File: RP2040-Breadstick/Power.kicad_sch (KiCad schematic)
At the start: 5 parts

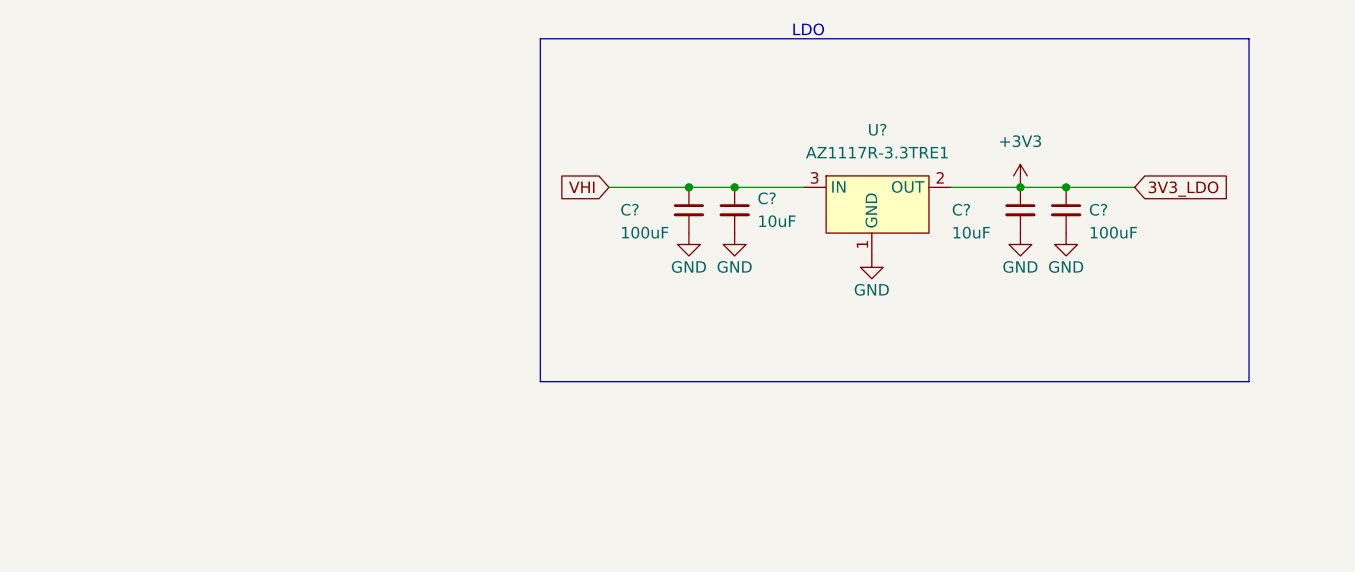
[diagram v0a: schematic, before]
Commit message: IMU Pins and Power Supply updated
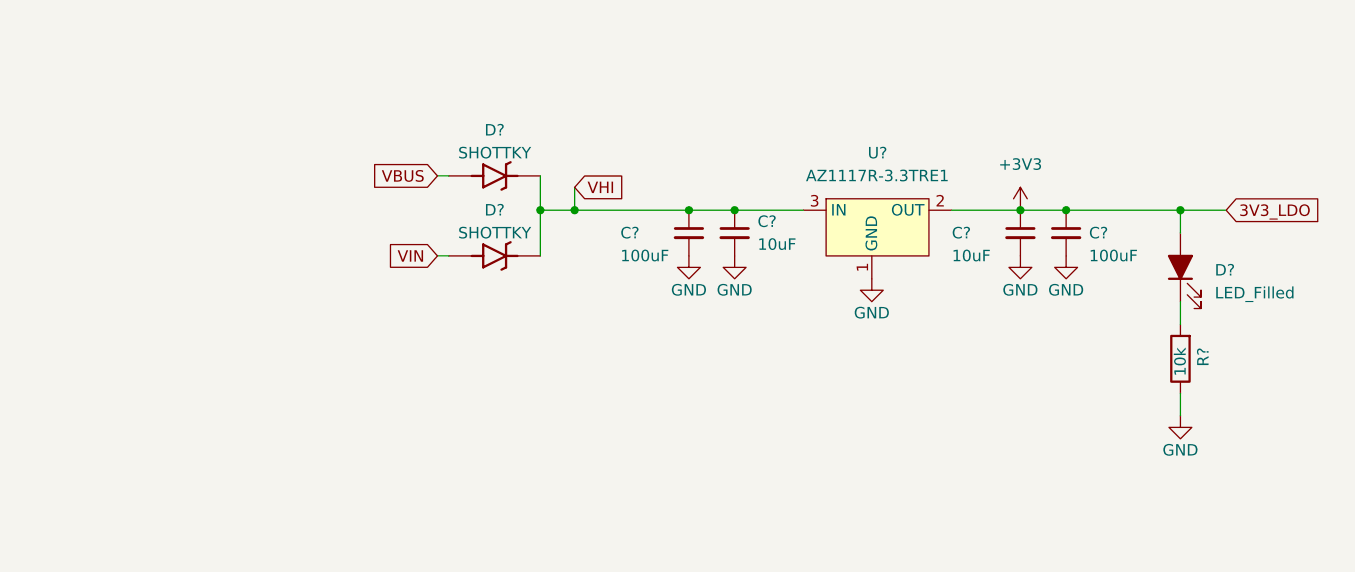
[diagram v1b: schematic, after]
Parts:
- added D? (x2): SHOTTKY, Diode_SMD:D_SOD-123, symbol SparkFun-DiscreteSemi:DIODE-SHOTTKY_MBRA140
- added D?: LED_Filled, LED_SMD:LED_0805_2012Metric, symbol Device:LED_Filled
- added R?: 10k, Breadstick Footprints:Perfect_0402_Resistor, symbol Device:R
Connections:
- net +3V3: now also D?.2 (A)
- net GND: now also R?.1
- net VHI: now also D?.1 (C), D?.1 (C)
- new net: D?.1 (K), R?.2
- new net VBUS: D?.2 (A)
- new net VIN: D?.2 (A)
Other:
- note removed: "LDO"
- moved on the sheet: C?, U?

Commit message: Schematic Rough Draft Complete
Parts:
- gave numbers to parts that had none: 9
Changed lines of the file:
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@@
   (symbol (lib_id "Device:C_Small") (at 137.16 97.79 0) (unit 1)
     (in_bom yes) (on_board yes)
-    (property "Reference" "C?" (id 0) (at 139.7 96.52 0)
+    (property "Reference" "C502" (id 0) (at 139.7 96.52 0)
       (effects (font (size 1.27 1.27)) (justify left))
     )
@@
   (symbol (lib_id "Device:C_Small") (at 168.91 97.79 0) (unit 1)
     (in_bom yes) (on_board yes)
-    (property "Reference" "C?" (id 0) (at 161.29 97.79 0)
+    (property "Reference" "C503" (id 0) (at 161.29 97.79 0)
       (effects (font (size 1.27 1.27)) (justify left))
     )
@@
   (symbol (lib_id "Device:R") (at 186.69 111.76 180) (unit 1)
     (in_bom yes) (on_board yes)
-    (property "Reference" "R?" (id 0) (at 189.23 110.49 90)
+    (property "Reference" "R501" (id 0) (at 189.23 110.49 90)
       (effects (font (size 1.27 1.27)) (justify left))
     )
@@
   (symbol (lib_id "power:GND") (at 132.08 100.33 0) (unit 1)
     (in_bom yes) (on_board yes)
-    (property "Reference" "#PWR?" (id 0) (at 132.08 106.68 0)
+    (property "Reference" "#PWR0502" (id 0) (at 132.08 106.68 0)
       (effects (font (size 1.27 1.27)) hide)
     )
@@
   (symbol (lib_id "power:GND") (at 173.99 100.33 0) (unit 1)
     (in_bom yes) (on_board yes)
-    (property "Reference" "#PWR?" (id 0) (at 173.99 106.68 0)
+    (property "Reference" "#PWR0505" (id 0) (at 173.99 106.68 0)
       (effects (font (size 1.27 1.27)) hide)
     )
@@
   (symbol (lib_name "DIODE-SHOTTKY_MBRA140_1") (lib_id "SparkFun-DiscreteSemi:DIODE-SHOTTKY_MBRA140") (at 110.49 91.44 0) (unit 1)
     (in_bom yes) (on_board yes)
-    (property "Reference" "D?" (id 0) (at 110.49 86.36 0))
+    (property "Reference" "D501" (id 0) (at 110.49 86.36 0))
     (property "Value" "SHOTTKY" (id 1) (at 110.49 88.9 0))
     (property "Footprint" "Diode_SMD:D_SOD-123" (id 2) (at 127 95.25 0)
@@
   (symbol (lib_id "Device:C_Small") (at 173.99 97.79 0) (unit 1)
     (in_bom yes) (on_board yes)
-    (property "Reference" "C?" (id 0) (at 176.53 97.79 0)
+    (property "Reference" "C504" (id 0) (at 176.53 97.79 0)
       (effects (font (size 1.27 1.27)) (justify left))
     )
@@
   (symbol (lib_name "DIODE-SHOTTKY_MBRA140_1") (lib_id "SparkFun-DiscreteSemi:DIODE-SHOTTKY_MBRA140") (at 110.49 100.33 0) (unit 1)
     (in_bom yes) (on_board yes)
-    (property "Reference" "D?" (id 0) (at 110.49 95.25 0))
+    (property "Reference" "D502" (id 0) (at 110.49 95.25 0))
     (property "Value" "SHOTTKY" (id 1) (at 110.49 97.79 0))
     (property "Footprint" "Diode_SMD:D_SOD-123" (id 2) (at 127 104.14 0)
@@
   (symbol (lib_id "power:GND") (at 152.4 102.87 0) (unit 1)
     (in_bom yes) (on_board yes)
-    (property "Reference" "#PWR?" (id 0) (at 152.4 109.22 0)
+    (property "Reference" "#PWR0506" (id 0) (at 152.4 109.22 0)
       (effects (font (size 1.27 1.27)) hide)
     )
@@
   (symbol (lib_id "power:GND") (at 168.91 100.33 0) (unit 1)
     (in_bom yes) (on_board yes)
-    (property "Reference" "#PWR?" (id 0) (at 168.91 106.68 0)
+    (property "Reference" "#PWR0504" (id 0) (at 168.91 106.68 0)
       (effects (font (size 1.27 1.27)) hide)
     )
@@
   (symbol (lib_id "power:GND") (at 137.16 100.33 0) (unit 1)
     (in_bom yes) (on_board yes)
-    (property "Reference" "#PWR?" (id 0) (at 137.16 106.68 0)
+    (property "Reference" "#PWR0503" (id 0) (at 137.16 106.68 0)
       (effects (font (size 1.27 1.27)) hide)
     )
@@
   (symbol (lib_id "power:+3V3") (at 168.91 95.25 0) (unit 1)
     (in_bom yes) (on_board yes) (fields_autoplaced)
-    (property "Reference" "#PWR?" (id 0) (at 168.91 99.06 0)
+    (property "Reference" "#PWR0501" (id 0) (at 168.91 99.06 0)
       (effects (font (size 1.27 1.27)) hide)
     )
@@
   (symbol (lib_id "BreadstickLibrary:AZ1117R-3.3TRE1") (at 152.4 96.52 0) (unit 1)
     (in_bom yes) (on_board yes) (fields_autoplaced)
-    (property "Reference" "U?" (id 0) (at 153.035 88.9 0))
+    (property "Reference" "U501" (id 0) (at 153.035 88.9 0))
     (property "Value" "AZ1117R-3.3TRE1" (id 1) (at 153.035 91.44 0))
     (property "Footprint" "Package_TO_SOT_SMD:SOT-89-3" (id 2) (at 152.4 96.52 0)
@@
   (symbol (lib_id "power:GND") (at 186.69 118.11 0) (unit 1)
     (in_bom yes) (on_board yes)
-    (property "Reference" "#PWR?" (id 0) (at 186.69 124.46 0)
+    (property "Reference" "#PWR0507" (id 0) (at 186.69 124.46 0)
       (effects (font (size 1.27 1.27)) hide)
     )
@@
   (symbol (lib_id "Device:C_Small") (at 132.08 97.79 0) (unit 1)
     (in_bom yes) (on_board yes)
-    (property "Reference" "C?" (id 0) (at 124.46 97.79 0)
+    (property "Reference" "C501" (id 0) (at 124.46 97.79 0)
       (effects (font (size 1.27 1.27)) (justify left))
     )
@@
   (symbol (lib_id "Device:LED_Filled") (at 186.69 101.6 90) (unit 1)
     (in_bom yes) (on_board yes) (fields_autoplaced)
-    (property "Reference" "D?" (id 0) (at 190.5 101.9174 90)
+    (property "Reference" "D503" (id 0) (at 190.5 101.9174 90)
       (effects (font (size 1.27 1.27)) (justify right))
     )

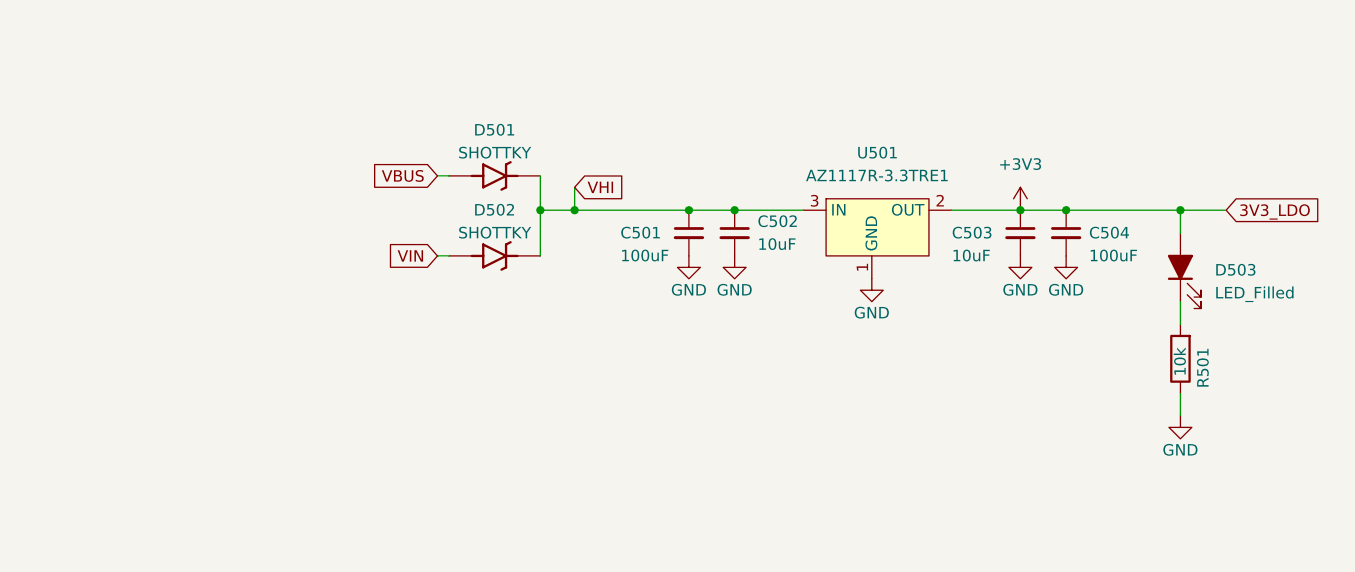
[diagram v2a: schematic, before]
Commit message: Initial PCB organization complete.
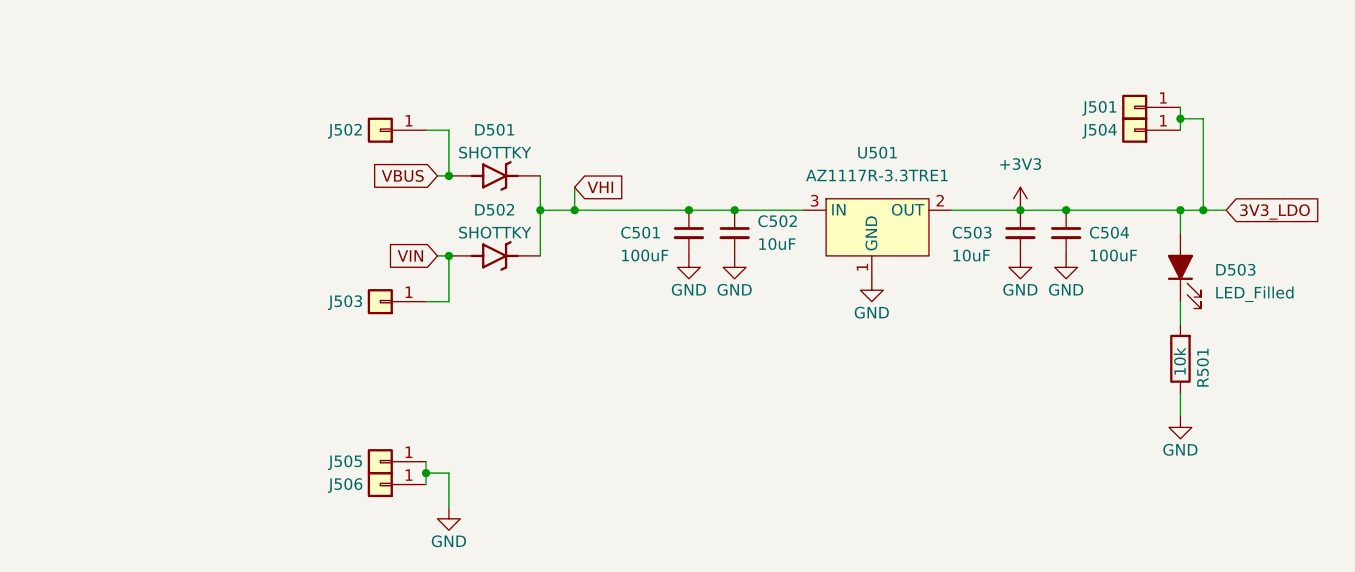
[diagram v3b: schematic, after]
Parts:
- added J501, J502, J503, J504, J505, J506: Conn_01x01, Connector_PinHeader_2.54mm:PinHeader_1x01_P2.54mm_Vertical, symbol Connector_Generic:Conn_01x01
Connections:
- net +3V3: now also J501.1 (Pin_1), J504.1 (Pin_1)
- net GND: now also J505.1 (Pin_1), J506.1 (Pin_1)
- net VBUS: now also J502.1 (Pin_1)
- net VIN: now also J503.1 (Pin_1)
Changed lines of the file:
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@@
   (junction (at 186.69 95.25) (diameter 0) (color 0 0 0 0)
   )
+  (junction (at 186.69 85.09) (diameter 0) (color 0 0 0 0)
+  )
   (junction (at 168.91 95.25) (diameter 0) (color 0 0 0 0)
   )
   (junction (at 137.16 95.25) (diameter 0) (color 0 0 0 0)
   )
+  (junction (at 105.41 91.44) (diameter 0) (color 0 0 0 0)
+  )
+  (junction (at 189.23 95.25) (diameter 0) (color 0 0 0 0)
+  )
+  (junction (at 105.41 100.33) (diameter 0) (color 0 0 0 0)
+  )
+  (junction (at 102.87 124.46) (diameter 0) (color 0 0 0 0)
+  )
   (junction (at 115.57 95.25) (diameter 0) (color 0 0 0 0)
   )
   (junction (at 132.08 95.25) (diameter 0) (color 0 0 0 0)
   )
-  (wire (pts (xy 186.69 95.25) (xy 191.77 95.25))
+  (wire (pts (xy 186.69 85.09) (xy 186.69 86.36))
+    (stroke (width 0) (type default) (color 0 0 0 0))
+  )
+  (wire (pts (xy 102.87 124.46) (xy 102.87 125.73))
+    (stroke (width 0) (type default) (color 0 0 0 0))
+  )
+  (wire (pts (xy 186.69 95.25) (xy 189.23 95.25))
     (stroke (width 0) (type default) (color 0 0 0 0))
   )
@@
     (stroke (width 0) (type default) (color 0 0 0 0))
   )
+  (wire (pts (xy 186.69 83.82) (xy 186.69 85.09))
+    (stroke (width 0) (type default) (color 0 0 0 0))
+  )
+  (wire (pts (xy 105.41 100.33) (xy 105.41 105.41))
+    (stroke (width 0) (type default) (color 0 0 0 0))
+  )
+  (wire (pts (xy 105.41 124.46) (xy 102.87 124.46))
+    (stroke (width 0) (type default) (color 0 0 0 0))
+  )
+  (wire (pts (xy 186.69 85.09) (xy 189.23 85.09))
+    (stroke (width 0) (type default) (color 0 0 0 0))
+  )
   (wire (pts (xy 115.57 95.25) (xy 115.57 100.33))
     (stroke (width 0) (type default) (color 0 0 0 0))
   )
+  (wire (pts (xy 102.87 105.41) (xy 105.41 105.41))
+    (stroke (width 0) (type default) (color 0 0 0 0))
+  )
+  (wire (pts (xy 189.23 85.09) (xy 189.23 95.25))
+    (stroke (width 0) (type default) (color 0 0 0 0))
+  )
   (wire (pts (xy 119.38 95.25) (xy 132.08 95.25))
     (stroke (width 0) (type default) (color 0 0 0 0))
   )
+  (wire (pts (xy 102.87 86.36) (xy 105.41 86.36))
+    (stroke (width 0) (type default) (color 0 0 0 0))
+  )
+  (wire (pts (xy 189.23 95.25) (xy 191.77 95.25))
+    (stroke (width 0) (type default) (color 0 0 0 0))
+  )
   (wire (pts (xy 186.69 95.25) (xy 186.69 97.79))
     (stroke (width 0) (type default) (color 0 0 0 0))
@@
     (stroke (width 0) (type default) (color 0 0 0 0))
   )
+  (wire (pts (xy 102.87 123.19) (xy 102.87 124.46))
+    (stroke (width 0) (type default) (color 0 0 0 0))
+  )
   (wire (pts (xy 104.14 91.44) (xy 105.41 91.44))
     (stroke (width 0) (type default) (color 0 0 0 0))
@@
   )
   (wire (pts (xy 137.16 95.25) (xy 144.78 95.25))
+    (stroke (width 0) (type default) (color 0 0 0 0))
+  )
+  (wire (pts (xy 105.41 86.36) (xy 105.41 91.44))
+    (stroke (width 0) (type default) (color 0 0 0 0))
+  )
+  (wire (pts (xy 105.41 128.27) (xy 105.41 124.46))
     (stroke (width 0) (type default) (color 0 0 0 0))
   )
@@
     (pin "2")
   )
+  (symbol (lib_id "Connector_Generic:Conn_01x01") (at 97.79 123.19 180) (unit 1)
+    (in_bom yes) (on_board yes)
+    (property "Reference" "J505" (id 0) (at 93.98 123.19 0))
+    (property "Value" "Conn_01x01" (id 1) (at 87.63 123.19 0)
+      (effects (font (size 1.27 1.27)) hide)
+    )
+    (property "Footprint" "Connector_PinHeader_2.54mm:PinHeader_1x01_P2.54mm_Vertical" (id 2) (at 97.79 123.19 0)
+      (effects (font (size 1.27 1.27)) hide)
+    )
+    (property "Datasheet" "~" (id 3) (at 97.79 123.19 0)
+      (effects (font (size 1.27 1.27)) hide)
+    )
+    (property "JLCPCB P/N" "C492400" (id 4) (at 97.79 123.19 0)
+      (effects (font (size 1.27 1.27)) hide)
+    )
+    (pin "1")
+  )
   (symbol (lib_id "Device:C_Small") (at 168.91 97.79 0) (unit 1)
     (in_bom yes) (on_board yes)
@@
     (pin "1")
     (pin "2")
+  )
+  (symbol (lib_id "Connector_Generic:Conn_01x01") (at 97.79 105.41 180) (unit 1)
+    (in_bom yes) (on_board yes)
+    (property "Reference" "J503" (id 0) (at 93.98 105.41 0))
+    (property "Value" "Conn_01x01" (id 1) (at 87.63 105.41 0)
+      (effects (font (size 1.27 1.27)) hide)
+    )
+    (property "Footprint" "Connector_PinHeader_2.54mm:PinHeader_1x01_P2.54mm_Vertical" (id 2) (at 97.79 105.41 0)
+      (effects (font (size 1.27 1.27)) hide)
+    )
+    (property "Datasheet" "~" (id 3) (at 97.79 105.41 0)
+      (effects (font (size 1.27 1.27)) hide)
+    )
+    (property "JLCPCB P/N" "C492400" (id 4) (at 97.79 105.41 0)
+      (effects (font (size 1.27 1.27)) hide)
+    )
+    (pin "1")
+  )
+  (symbol (lib_id "Connector_Generic:Conn_01x01") (at 181.61 83.82 180) (unit 1)
+    (in_bom yes) (on_board yes)
+    (property "Reference" "J501" (id 0) (at 177.8 83.82 0))
+    (property "Value" "Conn_01x01" (id 1) (at 171.45 83.82 0)
+      (effects (font (size 1.27 1.27)) hide)
+    )
+    (property "Footprint" "Connector_PinHeader_2.54mm:PinHeader_1x01_P2.54mm_Vertical" (id 2) (at 181.61 83.82 0)
+      (effects (font (size 1.27 1.27)) hide)
+    )
+    (property "Datasheet" "~" (id 3) (at 181.61 83.82 0)
+      (effects (font (size 1.27 1.27)) hide)
+    )
+    (property "JLCPCB P/N" "C492400" (id 4) (at 181.61 83.82 0)
+      (effects (font (size 1.27 1.27)) hide)
+    )
+    (pin "1")
+  )
+  (symbol (lib_id "Connector_Generic:Conn_01x01") (at 97.79 125.73 180) (unit 1)
+    (in_bom yes) (on_board yes)
+    (property "Reference" "J506" (id 0) (at 93.98 125.73 0))
+    (property "Value" "Conn_01x01" (id 1) (at 87.63 125.73 0)
+      (effects (font (size 1.27 1.27)) hide)
+    )
+    (property "Footprint" "Connector_PinHeader_2.54mm:PinHeader_1x01_P2.54mm_Vertical" (id 2) (at 97.79 125.73 0)
+      (effects (font (size 1.27 1.27)) hide)
+    )
+    (property "Datasheet" "~" (id 3) (at 97.79 125.73 0)
+      (effects (font (size 1.27 1.27)) hide)
+    )
+    (property "JLCPCB P/N" "C492400" (id 4) (at 97.79 125.73 0)
+      (effects (font (size 1.27 1.27)) hide)
+    )
+    (pin "1")
+  )
+  (symbol (lib_id "Connector_Generic:Conn_01x01") (at 181.61 86.36 180) (unit 1)
+    (in_bom yes) (on_board yes)
+    (property "Reference" "J504" (id 0) (at 177.8 86.36 0))
+    (property "Value" "Conn_01x01" (id 1) (at 171.45 86.36 0)
+      (effects (font (size 1.27 1.27)) hide)
+    )
+    (property "Footprint" "Connector_PinHeader_2.54mm:PinHeader_1x01_P2.54mm_Vertical" (id 2) (at 181.61 86.36 0)
+      (effects (font (size 1.27 1.27)) hide)
+    )
+    (property "Datasheet" "~" (id 3) (at 181.61 86.36 0)
+      (effects (font (size 1.27 1.27)) hide)
+    )
+    (property "JLCPCB P/N" "C492400" (id 4) (at 181.61 86.36 0)
+      (effects (font (size 1.27 1.27)) hide)
+    )
+    (pin "1")
   )
   (symbol (lib_id "power:GND") (at 132.08 100.33 0) (unit 1)
@@
     )
     (property "Datasheet" "" (id 3) (at 152.4 102.87 0)
+      (effects (font (size 1.27 1.27)) hide)
+    )
+    (pin "1")
+  )
+  (symbol (lib_id "Connector_Generic:Conn_01x01") (at 97.79 86.36 180) (unit 1)
+    (in_bom yes) (on_board yes)
+    (property "Reference" "J502" (id 0) (at 93.98 86.36 0))
+    (property "Value" "Conn_01x01" (id 1) (at 87.63 86.36 0)
+      (effects (font (size 1.27 1.27)) hide)
+    )
+    (property "Footprint" "Connector_PinHeader_2.54mm:PinHeader_1x01_P2.54mm_Vertical" (id 2) (at 97.79 86.36 0)
+      (effects (font (size 1.27 1.27)) hide)
+    )
+    (property "Datasheet" "~" (id 3) (at 97.79 86.36 0)
+      (effects (font (size 1.27 1.27)) hide)
+    )
+    (property "JLCPCB P/N" "C492400" (id 4) (at 97.79 86.36 0)
       (effects (font (size 1.27 1.27)) hide)
     )
@@
       (effects (font (size 1.27 1.27)) hide)
     )
+    (pin "1")
+  )
+  (symbol (lib_id "power:GND") (at 105.41 128.27 0) (unit 1)
+    (in_bom yes) (on_board yes)
+    (property "Reference" "#PWR0508" (id 0) (at 105.41 134.62 0)
+      (effects (font (size 1.27 1.27)) hide)
+    )
+    (property "Value" "GND" (id 1) (at 105.41 132.08 0))
+    (property "Footprint" "" (id 2) (at 105.41 128.27 0)
+      (effects (font (size 1.27 1.27)) hide)
+    )
+    (property "Datasheet" "" (id 3) (at 105.41 128.27 0)
+      (effects (font (size 1.27 1.27)) hide)
+    )
